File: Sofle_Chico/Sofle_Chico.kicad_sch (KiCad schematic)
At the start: 116 parts, among them J1 Conn_01x05, J2 MJ-4PP-9, J3 Conn_01x04, J4 Conn_01x04, J5 Conn_02x05_Odd_Even, J7 Conn_01x04, Q1 Si2301CDS, SW1 SW_PUSH, SW10 SW_PUSH, SW11 SW_PUSH, SW12 SW_PUSH, SW13 SW_PUSH, SW14 SW_PUSH, SW15 SW_PUSH, SW16 SW_PUSH, SW17 SW_PUSH, SW18 SW_PUSH, SW19 SW_PUSH, SW2 SW_PUSH, SW20 SW_PUSH, SW21 SW_PUSH, SW22 SW_PUSH, SW23 SW_PUSH, SW24 SW_PUSH, SW25 Rotary_Encoder_Switch-Device, SW26 SW_PUSH, SW27 SW_PUSH, SW28 SW_PUSH, SW29 SW_PUSH, SW3 SW_PUSH, SW30 SW_PUSH, SW4 SW_PUSH, SW5 SW_PUSH, SW6 SW_PUSH, SW7 SW_PUSH, SW8 SW_PUSH, SW9 SW_PUSH, U2 Pico

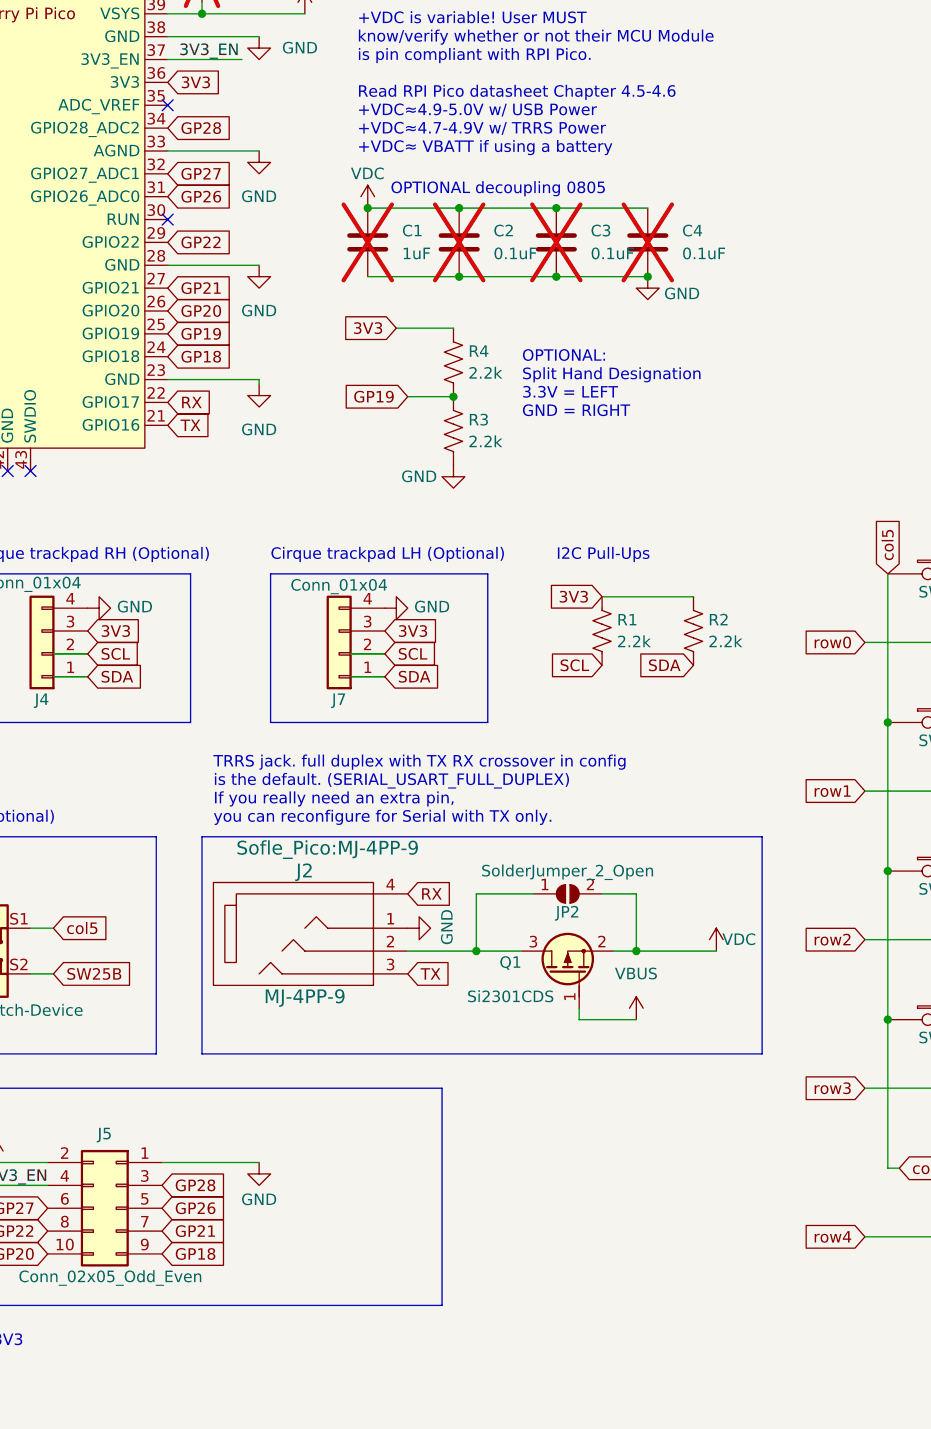
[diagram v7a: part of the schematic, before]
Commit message: Updated libraries for LED and socket hole resizing
i2c / handedness in place

silk fixes for VCC->3V3 labeling

Need to resize logos and swap in Chocs, but that requires KiCAD 8 upgrade so completing other work before the Rubicon
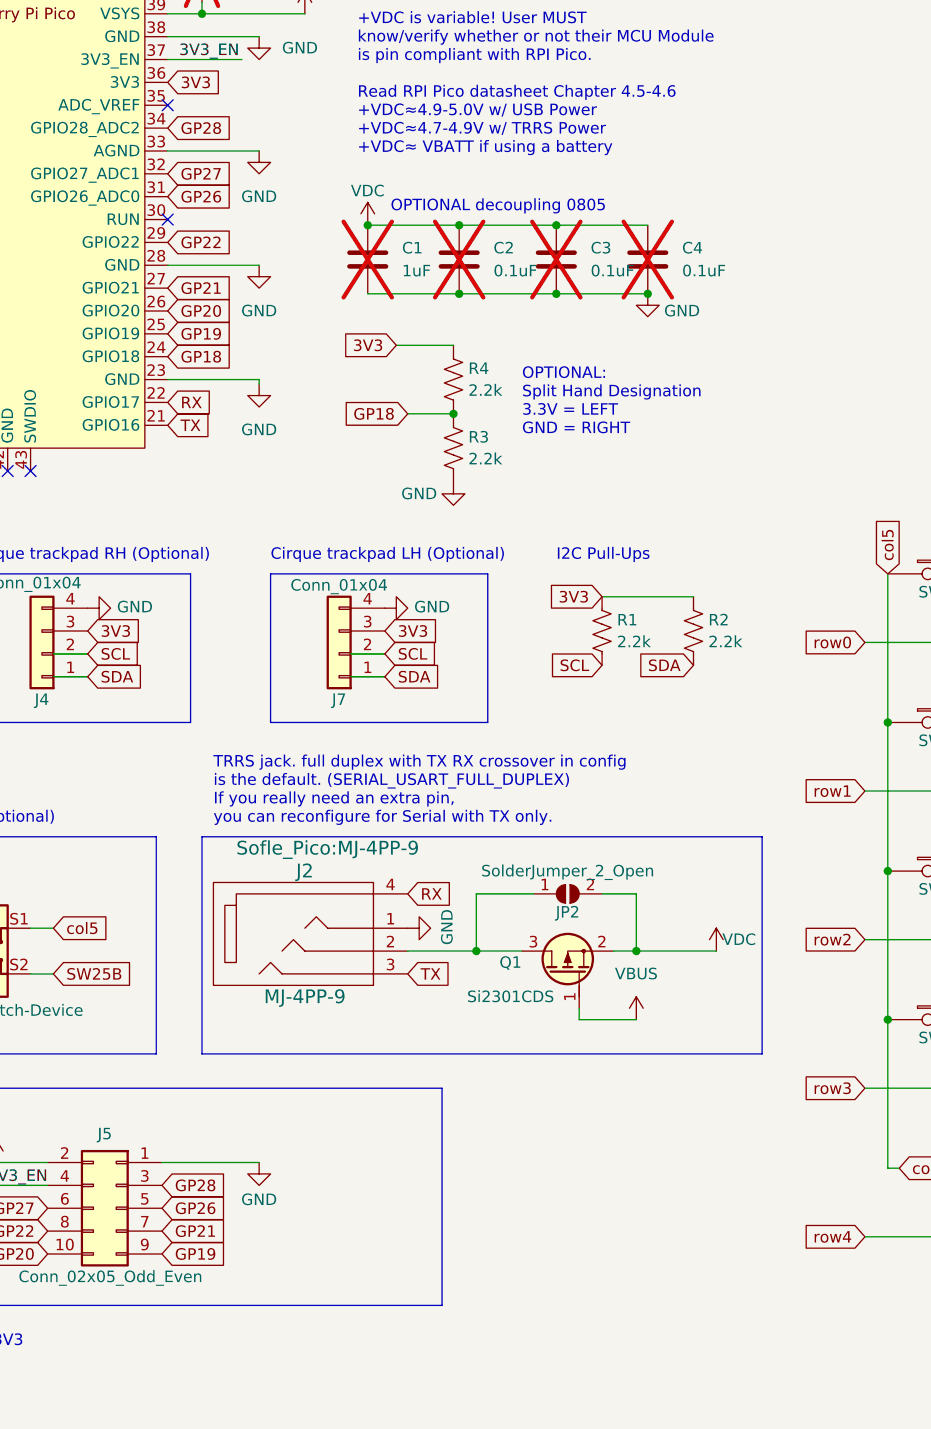
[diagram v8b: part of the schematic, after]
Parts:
- LED1, LED10, LED11, LED12, LED13, LED14, LED15, LED16, LED17, LED18, LED19, LED2, LED20, LED21, LED22, LED23, LED24, LED25, LED26, LED27, LED28, LED29, LED3, LED4, LED5, LED6, LED7, LED8, LED9: footprint Sofle_Pico:SK6803_MINI-E_V2 -> Sofle_Pico:SK6803_MINI-E_v3.5.5
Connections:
- net GP18: now also R3.1, R4.1; no longer J5.9 (Pin_9)
- net GP19: now also J5.9 (Pin_9); no longer R3.1, R4.1
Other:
- moved on the sheet: C1, C2, C3, C4, R3, R4
